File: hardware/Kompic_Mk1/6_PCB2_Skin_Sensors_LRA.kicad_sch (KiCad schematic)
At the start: 21 parts, among them CN2 Qvar_Electrode_1, J3 DB-Interface, M1 ELV1411A, U13 MAX30101EFD+T, U14 DRV2605LDGSR, U15 TMP117AIDRVR

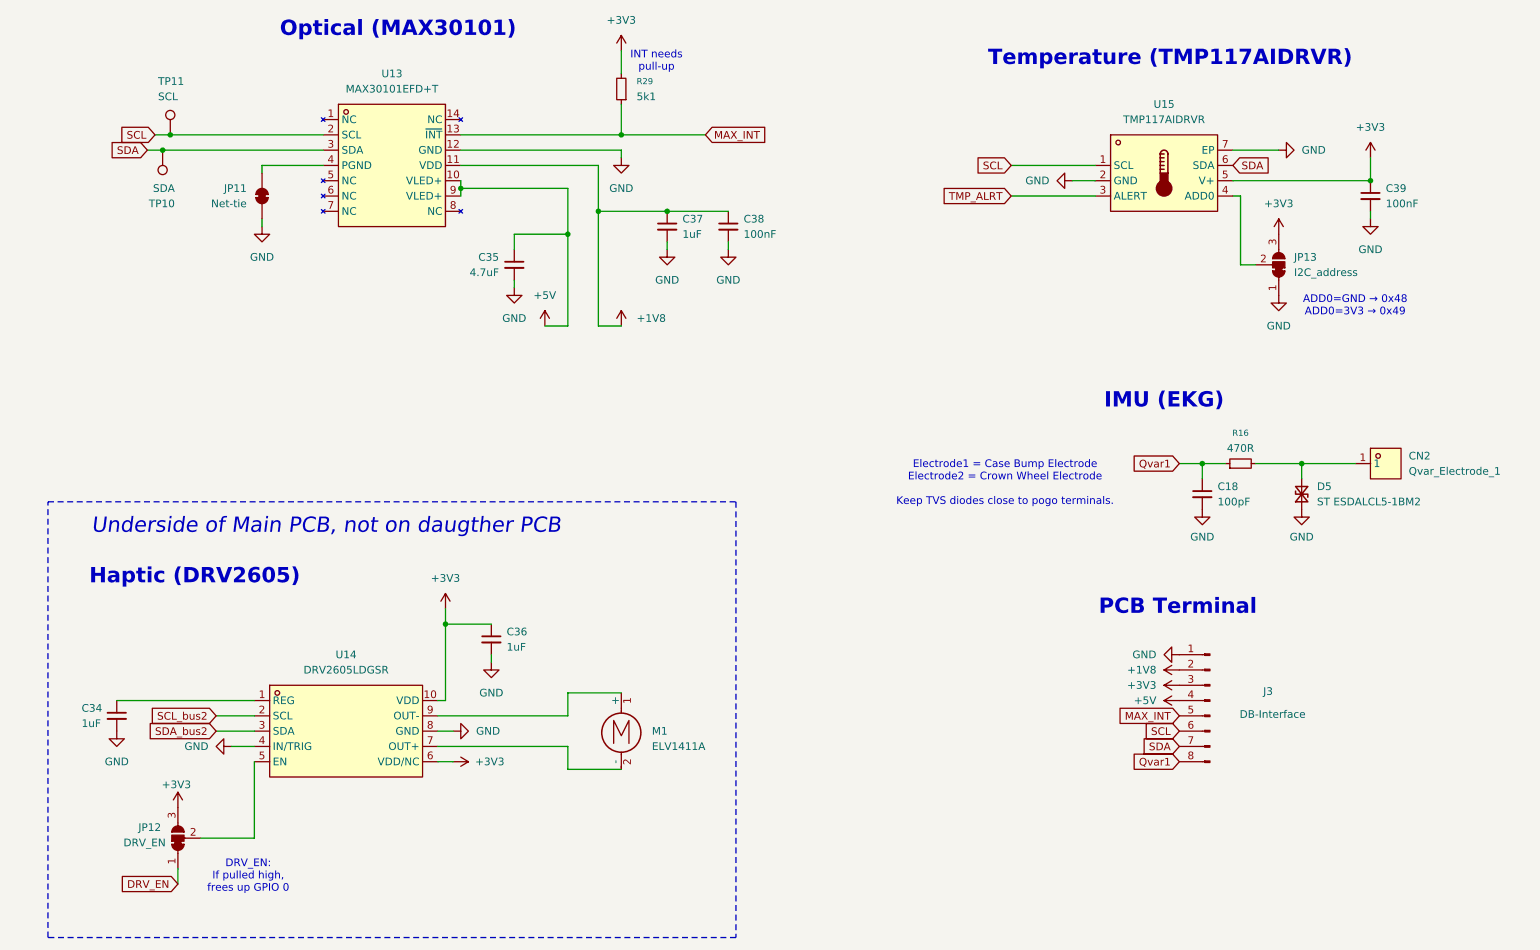
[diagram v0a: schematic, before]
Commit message: BIG CHANGE: Had bad wiring for the AMOLED, had to redo the schematic and complete routing of PCB (iv7.1). Added Arduino sketch for verifying AMOLED. Added newly redone pinout for both ESP32-S3 and the AMOLED.
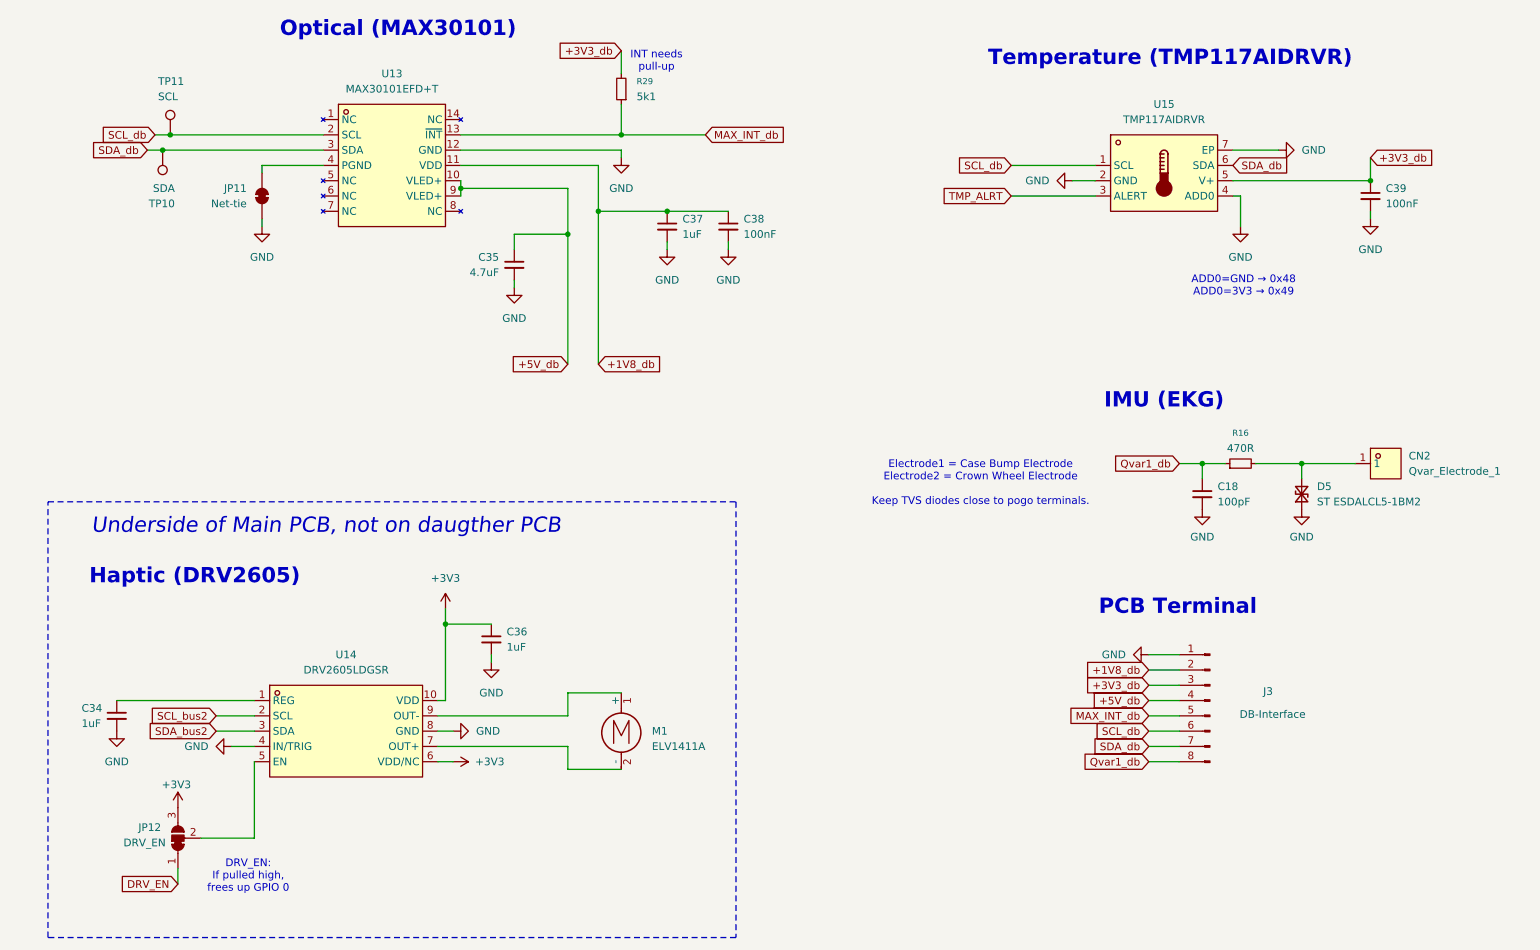
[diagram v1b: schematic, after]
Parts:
- removed JP13: I2C_address, Jumper:SolderJumper-3_P1.3mm_Bridged2Bar12_RoundedPad1.0x1.5mm, symbol Jumper:SolderJumper_3_Bridged12
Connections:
- net +3V3: no longer C39.1, J3.3 (Pin_3), R29.2, U15.5 (V+)
- net GND: now also U15.4 (ADD0)
- net +1V8 renamed +1V8_db
- net +5V renamed +5V_db
- net MAX_INT renamed MAX_INT_db
- net Qvar1 renamed Qvar1_db
- net SCL renamed SCL_db
- net SDA renamed SDA_db
- new net +3V3_db: C39.1, J3.3 (Pin_3), R29.2, U15.5 (V+)

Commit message: Added Circuit page! Minor touchups to schematic + Schematic PDF.
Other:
- company: Ivan Porupski May2026(c) -> Ivan Porupski June2026(c)
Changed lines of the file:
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@@
 	(paper "A4")
 	(title_block
-		(date "2026-05-30")
+		(date "2026-06-02")
 		(rev "iv7.1")
-		(company "Ivan Porupski May2026(c)")
+		(company "Ivan Porupski June2026(c)")
 	)
 	(rectangle
